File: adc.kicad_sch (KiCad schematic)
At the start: 14 parts, among them U6 TPS7B91050DBVR, U7 ADS7253

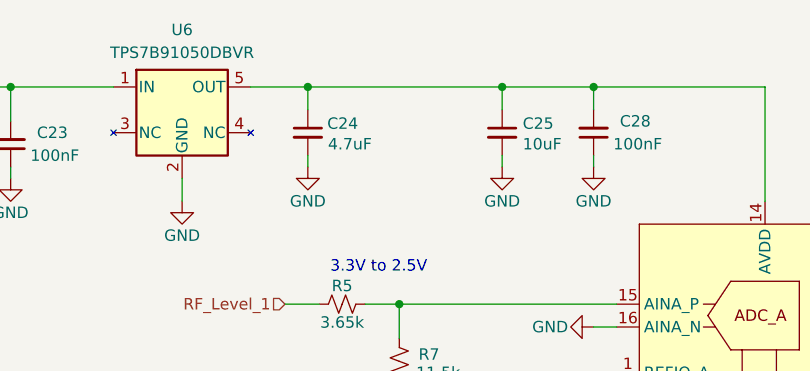
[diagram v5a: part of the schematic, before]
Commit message: Updated Footprint of Connectors
-Added a 0 ohm resistor after the 5V LDO
- fixed some part numbers
- adding 3d model to the isorate connectors
- updated datasheet/design docs
- changed one of the DIO connector to a vertical connector
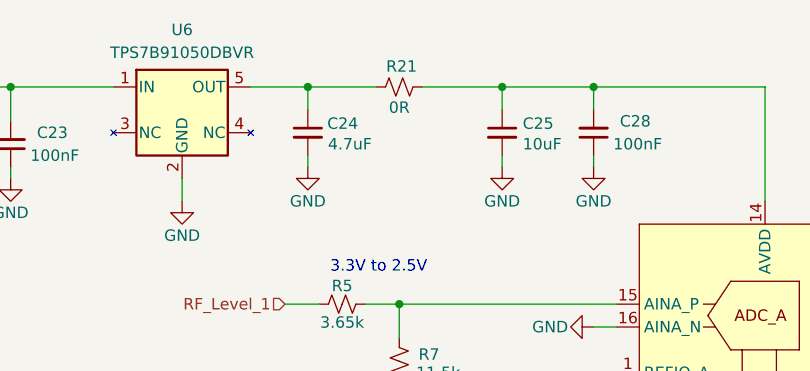
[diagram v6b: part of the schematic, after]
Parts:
- added R21: 0R, Resistor_SMD:R_0805_2012Metric, symbol Device:R_Small_US
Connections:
- net at C25.1, C28.2, U7.14 (AVDD): now also R21.2; no longer C24.1, U6.5 (OUT)
- new net: C24.1, R21.1, U6.5 (OUT)
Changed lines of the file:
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@@
+	)
+	(junction
+		(at 102.87 91.44)
+		(diameter 0)
+		(color 0 0 0 0)
+	)
+	(junction
+		(at 124.46 67.31)
+		(diameter 0)
+		(color 0 0 0 0)
+	)
+	(junction
+		(at 59.69 67.31)
+		(diameter 0)
+		(color 0 0 0 0)
+	)
+	(junction
+		(at 168.91 67.31)
+		(diameter 0)
+		(color 0 0 0 0)
 	)
 	(junction
@@
 	)
 	(junction
-		(at 102.87 91.44)
-		(diameter 0)
-		(color 0 0 0 0)
-	)
-	(junction
-		(at 124.46 67.31)
-		(diameter 0)
-		(color 0 0 0 0)
-	)
-	(junction
-		(at 59.69 67.31)
-		(diameter 0)
-		(color 0 0 0 0)
-	)
-	(junction
-		(at 168.91 67.31)
-		(diameter 0)
-		(color 0 0 0 0)
-	)
-	(junction
 		(at 114.3 67.31)
 		(diameter 0)
@@
 	(wire
 		(pts
+			(xy 92.71 67.31) (xy 100.33 67.31)
+		)
+		(stroke
+			(width 0)
+			(type default)
+		)
+	)
+	(wire
+		(pts
 			(xy 179.07 67.31) (xy 189.23 67.31)
 		)
@@
 	(wire
 		(pts
+			(xy 105.41 67.31) (xy 114.3 67.31)
+		)
+		(stroke
+			(width 0)
+			(type default)
+		)
+	)
+	(wire
+		(pts
 			(xy 127 106.68) (xy 120.65 106.68)
 		)
@@
 		(pts
 			(xy 99.06 91.44) (xy 102.87 91.44)
-		)
-		(stroke
-			(width 0)
-			(type default)
-		)
-	)
-	(wire
-		(pts
-			(xy 92.71 67.31) (xy 114.3 67.31)
 		)
 		(stroke
@@
 					(unit 1)
 				)
+			)
+		)
+	)
+	(symbol
+		(lib_id "Device:R_Small_US")
+		(at 102.87 67.31 90)
+		(unit 1)
+		(exclude_from_sim no)
+		(in_bom yes)
+		(on_board yes)
+		(dnp no)
+		(property "Reference" "R21"
+			(at 103.124 65.024 90)
+			(effects
+				(font
+					(size 1.27 1.27)
+				)
+			)
+		)
+		(property "Value" "0R"
+			(at 102.87 69.596 90)
+			(effects
+				(font
+					(size 1.27 1.27)
+				)
+			)
+		)
+		(property "Footprint" "Resistor_SMD:R_0805_2012Metric"
+			(at 102.87 67.31 0)
+			(effects
+				(font
+					(size 1.27 1.27)
+				)
+				(hide yes)
+			)
+		)
+		(property "Datasheet" "~"
+			(at 102.87 67.31 0)
+			(effects
+				(font
+					(size 1.27 1.27)
+				)
+				(hide yes)
+			)
+		)
+		(property "Description" ""
+			(at 102.87 67.31 0)
+			(effects
+				(font
+					(size 1.27 1.27)
+				)
+				(hide yes)
+			)
+		)
+		(property "MPN" "ERJ-6GEY0R00V"
+			(at 102.87 67.31 0)
+			(effects
+				(font
+					(size 1.27 1.27)
+				)
+				(hide yes)
+			)
+		)
+		(property "Manufacturer" "Panasonic Electronic Components"
+			(at 102.87 67.31 0)
+			(effects
+				(font
+					(size 1.27 1.27)
+				)
+				(hide yes)
+			)
+		)
+		(pin "1"
+		)
+		(pin "2"
+		)
+		(instances
+			(project "rf-input-fmc"
+				(path "/1719e569-47c8-4fa0-8523-9c9686ef0dba/d098b615-7cba-44eb-be59-7a71f2f48c2b"
+					(reference "R21")
+					(unit 1)
+				)

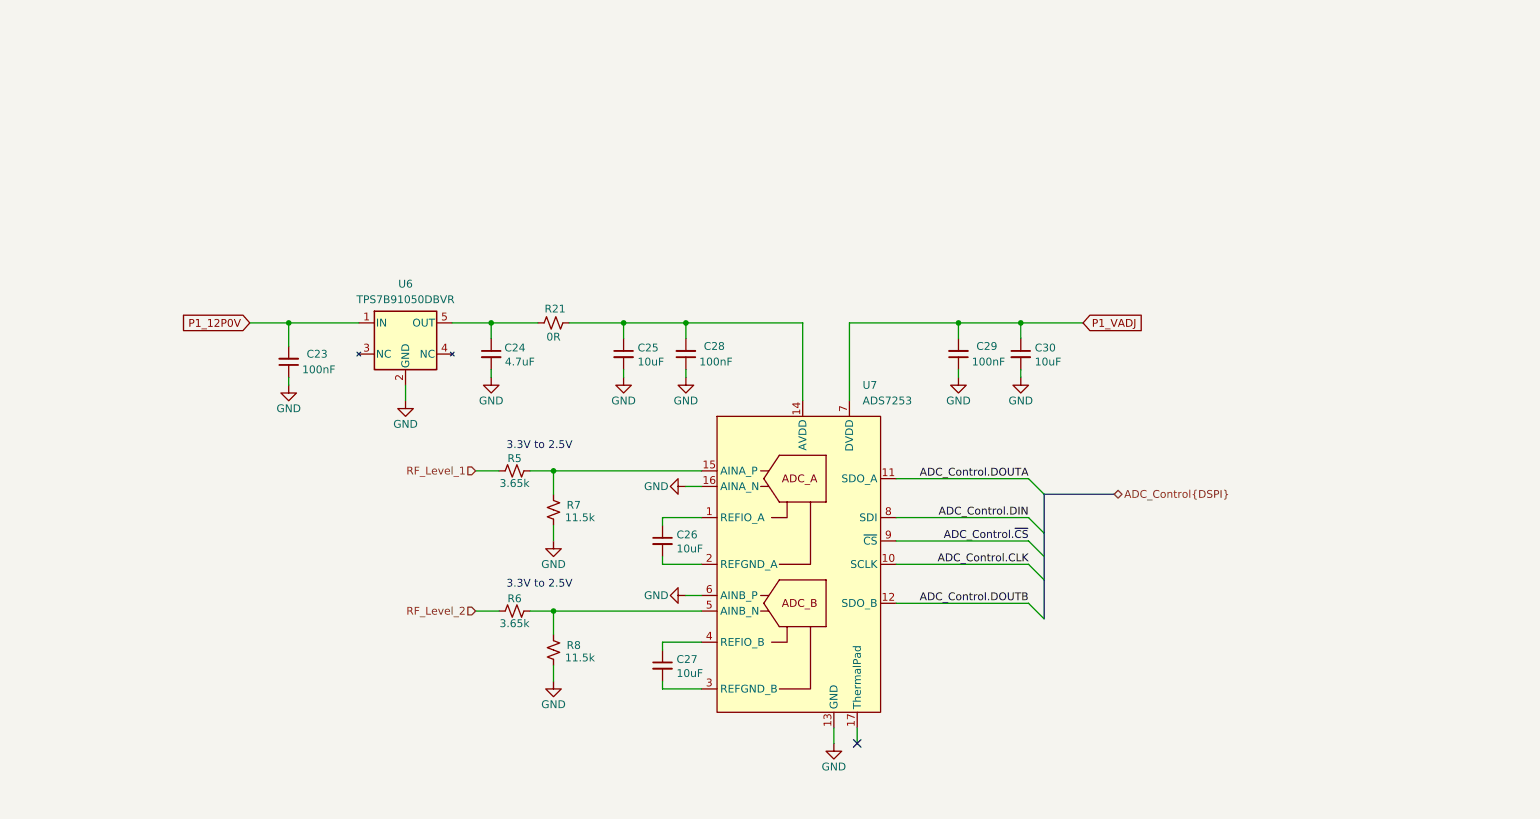
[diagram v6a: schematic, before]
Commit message: Schematic updates
- Changed Connecters to MMCX
- Added Test points on clocks and data buses
- Added attenuation before the RF input level detection IC to better keep the recommended input within its linear range
- Added a low pass filter at the input of the RF input level detection IC
- grounded the thermal pad of the ADC
- added some additional decoupling caps in for the clock splitter chip (to be in line with what is on Zest)
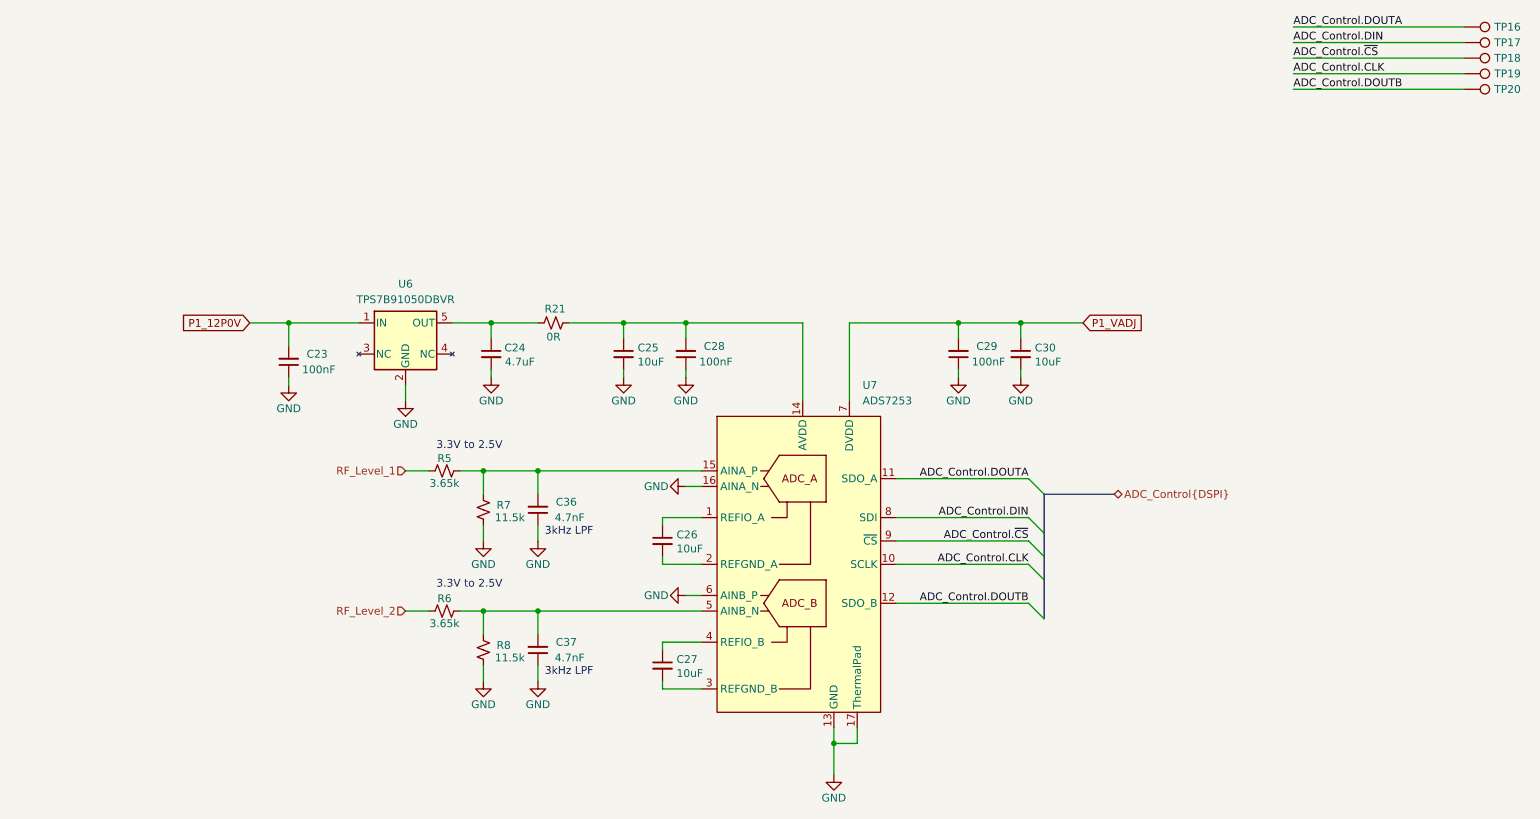
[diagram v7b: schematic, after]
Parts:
- added C36, C37: 4.7nF, Capacitor_SMD:C_0402_1005Metric, symbol Device:C_Small
- added TP16, TP17, TP18, TP19, TP20: TestPoint, TestPoint:TestPoint_Pad_D1.0mm, symbol Connector:TestPoint
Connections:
- net ADC_Control.CLK: now also TP19.1
- net ADC_Control.DIN: now also TP17.1
- net ADC_Control.DOUTA: now also TP16.1
- net ADC_Control.DOUTB: now also TP20.1
- net ADC_Control.~{CS}: now also TP18.1
- net GND: now also U7.17 (ThermalPad), C36.1, C37.1
- net at R5.2, R7.2, U7.15 (AINA_P): now also C36.2
- net at R6.2, R8.2, U7.5 (AINB_N): now also C37.2
- no-connect marks 1 -> 0
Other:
- note added: "3kHz LPF"
- moved on the sheet: R5, R6, R7, R8

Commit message: Updated BOM of all parts
Updated BOM of all parts
-added supplier & supplier part number to all parts
- fixed many issues with part including:R5-R8,C34,C35,C24, R10-R15

Changed filter C36&C37 to 15nF (keep COG & 0603, but changes filter cutoff to 3.8kHz|was 12kHz)
Changed bulk Caps to 22uF (was 47uF) to get a Cap with enough voltage headroom at 12V while 0805
Changed C31 to be a bulk 10uF cap
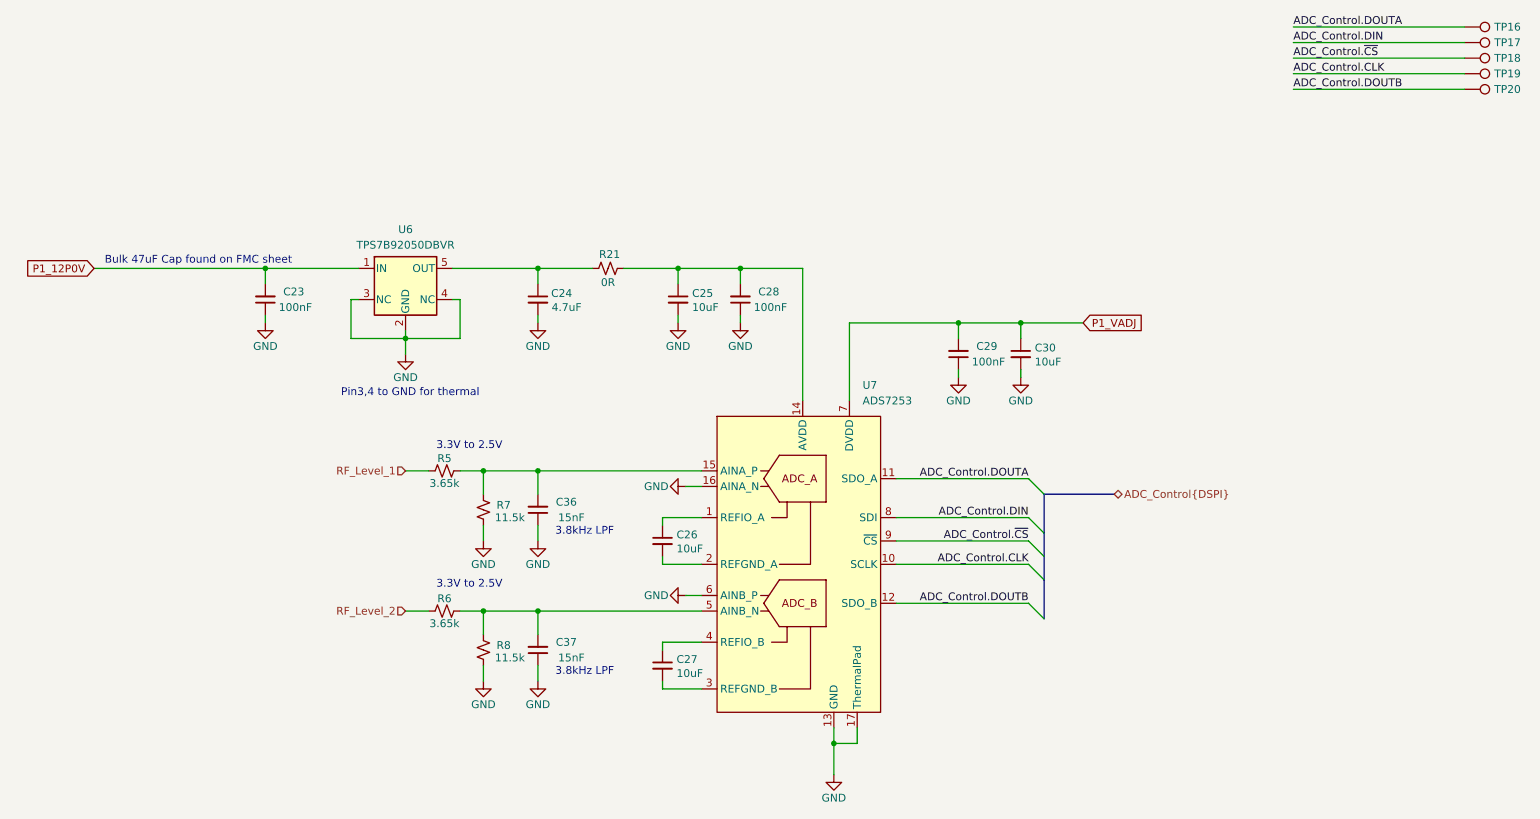
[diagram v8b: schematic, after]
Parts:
- C23, C28, C29: MPN GRM155R61A104KA01D -> GCM155R71H104KE02J; Manufacturer Murata -> Murata Electronics; Supplier (none) -> Digikey; Supplier Part Number (none) -> 490-14514-1-ND
- C24: MPN CC0603KRX7R7BB105 -> GRM188R61E475KE11D; Manufacturer YAGEO -> Murata Electronics; Supplier (none) -> Digikey; Supplier Part Number (none) -> 490-7203-1-ND
- C25, C26, C27, C30: Supplier (none) -> Digikey; Supplier Part Number (none) -> 490-13248-1-ND
- C36, C37: value 4.7nF -> 15nF; footprint Capacitor_SMD:C_0402_1005Metric -> Capacitor_SMD:C_0603_1608Metric; MPN GRM1555C1H472JE01D -> C1608C0G1V153J080AC; Manufacturer Murata Electronics -> TDK Corporation; Supplier (none) -> Digikey; Supplier Part Number (none) -> 445-174557-1-ND
- R21: Supplier (none) -> Digikey; Supplier Part Number (none) -> P0.0ACT-ND
- R5, R6: footprint Resistor_SMD:R_0402_1005Metric -> Resistor_SMD:R_0603_1608Metric_Pad0.98x0.95mm_HandSolder; MPN RC0603FR-07475RL -> RC0603FR-073K65L; Supplier (none) -> Digikey; Supplier Part Number (none) -> 311-3.65KHRCT-ND
- R7, R8: footprint Resistor_SMD:R_0402_1005Metric -> Resistor_SMD:R_0603_1608Metric_Pad0.98x0.95mm_HandSolder; MPN RC0603FR-07475RL -> RC0603FR-0711K5L; Supplier (none) -> Digikey; Supplier Part Number (none) -> 311-11.5KHRCT-ND
- TP16, TP17, TP18, TP19, TP20: now left out of the parts list
- U6: value TPS7B91050DBVR -> TPS7B92050DBVR; Supplier (none) -> Digikey; Supplier Part Number (none) -> 296-TPS7B92050DBVRCT-ND
- U7: footprint Package_DFN_QFN:Texas_RTE0016D_WQFN-16-1EP_3x3mm_P0.5mm_EP0.8x0.8mm_ThermalVias -> rf-input-fmc:Texas_RTE0016D_WQFN-16-1EP_3x3mm_P0.5mm_EP0.8x0.8mm_ThermalVias; Supplier (none) -> Digikey; Supplier Part Number (none) -> 296-38482-1-ND
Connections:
- net GND: now also U6.3 (NC), U6.4 (NC)
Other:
- note added: "3.8kHz LPF"
- note added: "Bulk 47uF Cap found on FMC sheet"
- note added: "Pin3,4 to GND for thermal"
- note removed: "3kHz LPF"
- moved on the sheet: C23, C24, C25, C28, R21
